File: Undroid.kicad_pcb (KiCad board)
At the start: 4 copper layers, 64.1 x 143 mm, 0 parts

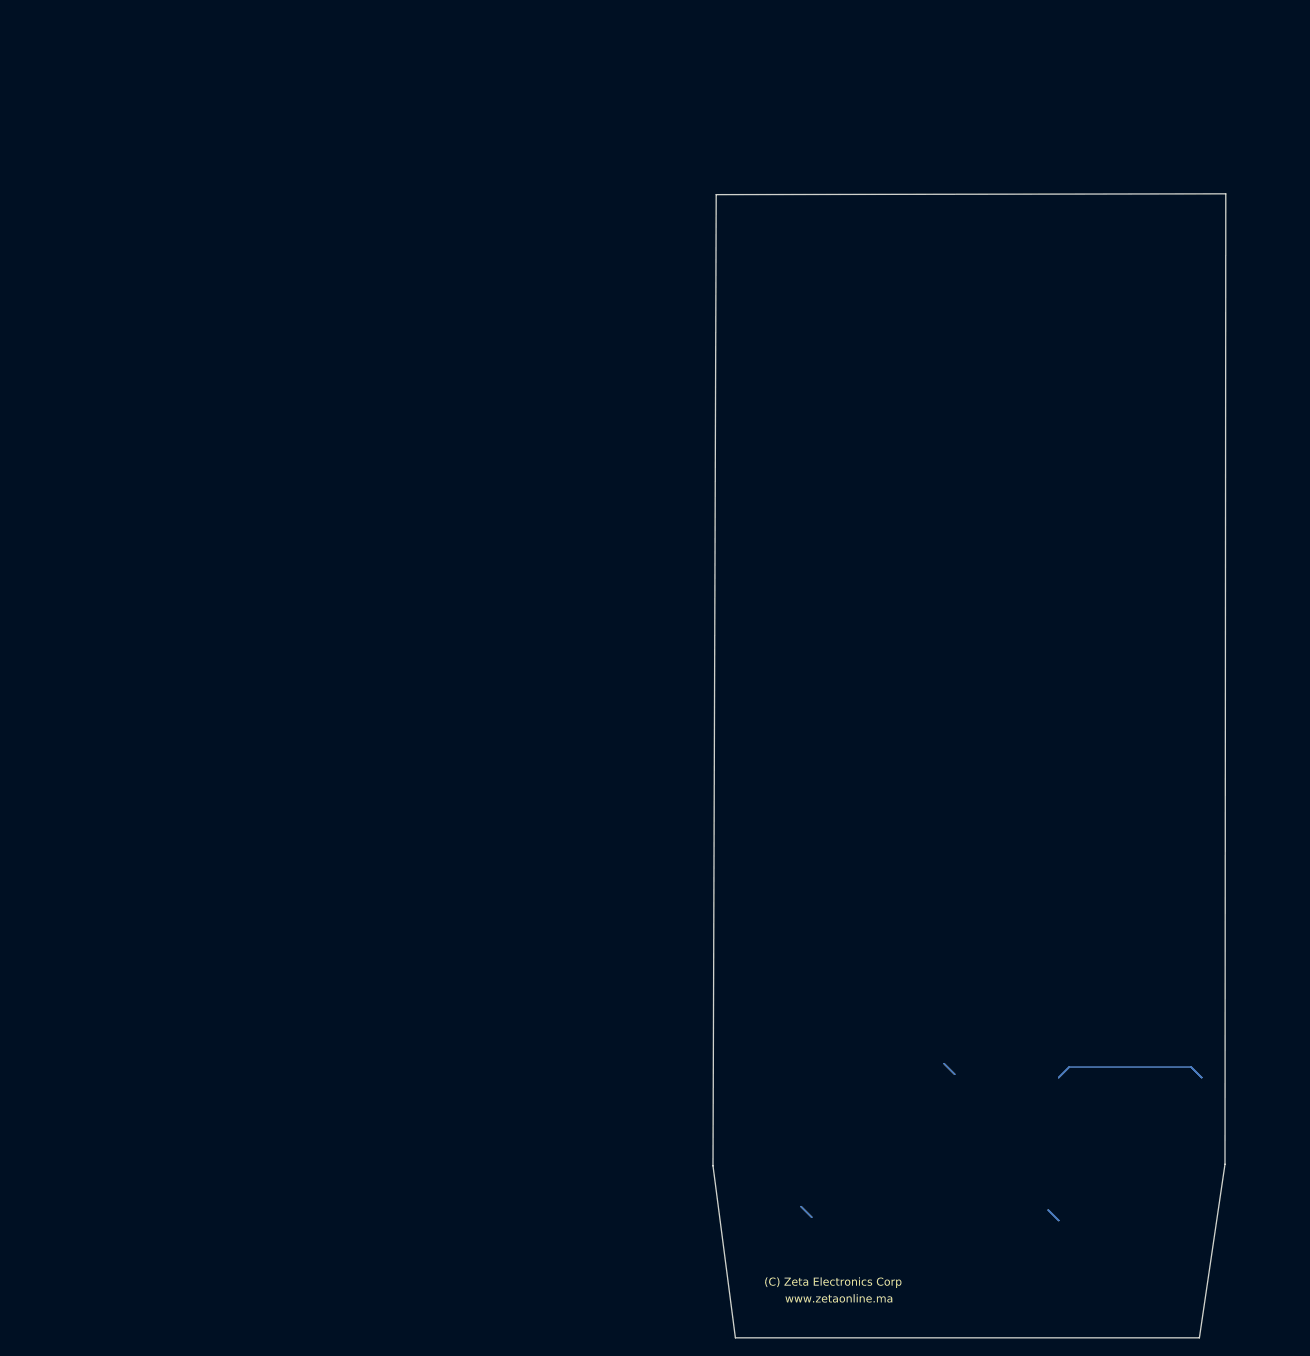
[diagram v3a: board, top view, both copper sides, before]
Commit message: fix: Include part of Allwinner SoC. fix: Fix ERC and DRC.
Signed-off-by: Amlal EL Mahrouss <amlalelmahrouss@icloud.com>
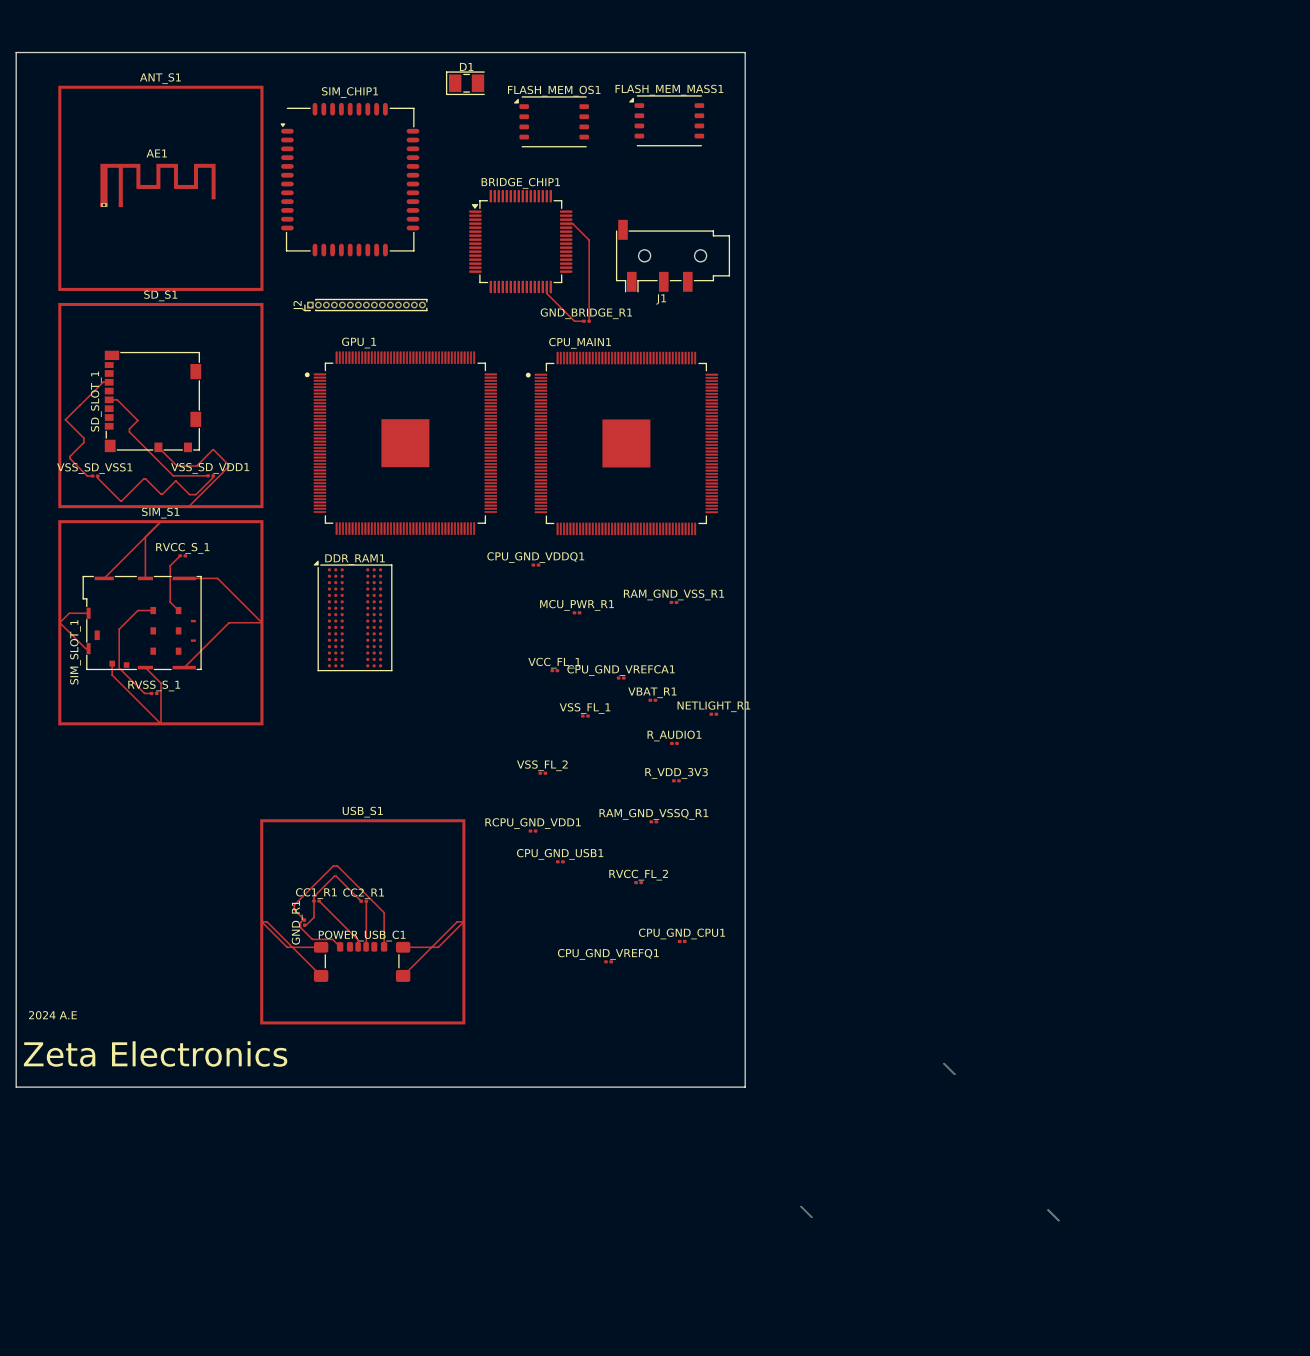
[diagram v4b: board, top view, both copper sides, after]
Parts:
- added AE1: Antenna_Shield, RF_Antenna:Texas_SWRA117D_2.4GHz_Right, F.Cu at (36.7, 39.8)
- added ANT_S1: RFShield_OnePiece, RF_Shielding:Laird_Technologies_97-2002_25.40x25.40mm, F.Cu at (41.7, 37.7)
- added BRIDGE_CHIP1: ATSAME70J19A-AN, Package_QFP:LQFP-64_10x10mm_P0.5mm, F.Cu at (86.7, 44.4)
- added CC1_R1: R, Resistor_SMD:R_0201_0603Metric, F.Cu at (61.1, 126.8)
- added CC2_R1: R, Resistor_SMD:R_0201_0603Metric, F.Cu at (67.0, 126.8)
- added CPU_GND_CPU1: R, Resistor_SMD:R_0201_0603Metric, F.Cu at (106.8, 131.8)
- added CPU_GND_USB1: R, Resistor_SMD:R_0201_0603Metric, F.Cu at (91.6, 121.9)
- added CPU_GND_VDDQ1: R, Resistor_SMD:R_0201_0603Metric, F.Cu at (88.6, 84.8)
- added CPU_GND_VREFCA1: R, Resistor_SMD:R_0201_0603Metric, F.Cu at (99.2, 98.9)
- added CPU_GND_VREFQ1: R, Resistor_SMD:R_0201_0603Metric, F.Cu at (97.6, 134.4)
- added CPU_MAIN1: Allwinner-A13, Allwinner:QFP40P2200X2200X160-177N, F.Cu at (99.9, 69.6)
- added D1: LED, LED_SMD:LED_PLCC-2_3x2mm_AK, F.Cu at (79.9, 24.6)
- added DDR_RAM1: AS4C256M16D3, Package_BGA:BGA-96_9.0x13.0mm_Layout2x3x16_P0.8mm, F.Cu at (66.0, 91.4)
- added FLASH_MEM_MASS1: XTSD08G, Package_LGA:LGA-8_8x6mm_P1.27mm, F.Cu at (105.2, 29.3)
- added FLASH_MEM_OS1: XTSD08G, Package_LGA:LGA-8_8x6mm_P1.27mm, F.Cu at (90.8, 29.4)
- added GND_BRIDGE_R1: R, Resistor_SMD:R_0201_0603Metric, F.Cu at (94.9, 54.3)
- added GND_R1: R, Resistor_SMD:R_0201_0603Metric, F.Cu at (59.6, 129.5)
- added GPU_1: Allwinner-A13, Allwinner:QFP40P2200X2200X160-177N, F.Cu at (72.2, 69.6)
- added J1: AudioJack2, Connector_Audio:Jack_3.5mm_PJ320D_Horizontal, F.Cu at (104.4, 46.1)
- added J2: Conn_01x15, Connector_PinHeader_1.00mm:PinHeader_1x15_P1.00mm_Vertical, F.Cu at (60.4, 52.3)
- added MCU_PWR_R1: R, Resistor_SMD:R_0201_0603Metric, F.Cu at (93.7, 90.8)
- added NETLIGHT_R1: R, Resistor_SMD:R_0201_0603Metric, F.Cu at (110.8, 103.5)
- added POWER_USB_C1: USB_C_Receptacle_PowerOnly_6P, Connector_USB:USB_C_Receptacle_GCT_USB4135-GF-A_6P_TopMnt_Horizontal, F.Cu at (66.8, 135.6)
- added RAM_GND_VSSQ_R1: R, Resistor_SMD:R_0201_0603Metric, F.Cu at (103.3, 116.9)
- added RAM_GND_VSS_R1: R, Resistor_SMD:R_0201_0603Metric, F.Cu at (105.8, 89.5)
- added RCPU_GND_VDD1: R, Resistor_SMD:R_0201_0603Metric, F.Cu at (88.2, 118.0)
- added RVCC_FL_2: R, Resistor_SMD:R_0201_0603Metric, F.Cu at (101.4, 124.5)
- added RVCC_S_1: R, Resistor_SMD:R_0201_0603Metric, F.Cu at (44.4, 83.7)
- added RVSS_S_1: R, Resistor_SMD:R_0201_0603Metric, F.Cu at (40.9, 100.8)
- added R_AUDIO1: R, Resistor_SMD:R_0201_0603Metric, F.Cu at (105.9, 107.1)
- added R_VDD_3V3: R, Resistor_SMD:R_0201_0603Metric, F.Cu at (106.1, 111.8)
- added SD_S1: RFShield_OnePiece, RF_Shielding:Laird_Technologies_97-2002_25.40x25.40mm, F.Cu at (41.7, 64.9)
- added SD_SLOT_1: Micro_SD_Card, Connector_Card:microSD_HC_Molex_104031-0811, F.Cu at (40.7, 64.3)
- added SIM_CHIP1: SIM7020C, RF_GSM:SIMCom_SIM800C, F.Cu at (65.3, 36.6)
- added SIM_S1: RFShield_OnePiece, RF_Shielding:Laird_Technologies_97-2002_25.40x25.40mm, F.Cu at (41.7, 92.0)
- added SIM_SLOT_1: JAE_SIM_Card_SF72S006, Connector_JAE:JAE_SIM_Card_SF72S006, F.Cu at (41.4, 93.0)
- added USB_S1: RFShield_OnePiece, RF_Shielding:Laird_Technologies_97-2002_25.40x25.40mm, F.Cu at (66.9, 129.4)
- added VBAT_R1: R, Resistor_SMD:R_0201_0603Metric, F.Cu at (103.2, 101.7)
- added VCC_FL_1: R, Resistor_SMD:R_0201_0603Metric, F.Cu at (90.9, 98.0)
- added VSS_FL_1: R, Resistor_SMD:R_0201_0603Metric, F.Cu at (94.8, 103.7)
- added VSS_FL_2: R, Resistor_SMD:R_0201_0603Metric, F.Cu at (89.4, 110.8)
- added VSS_SD_VDD1: R, Resistor_SMD:R_0201_0603Metric, F.Cu at (47.9, 73.7)
- added VSS_SD_VSS1: R, Resistor_SMD:R_0201_0603Metric, F.Cu at (33.5, 73.7)
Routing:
- net Net-(SIM_S1-Shield): track 0.00 -> 68.9 mm
- net Net-(POWER_USB_C1-SHIELD): track 0.00 -> 38.3 mm
- net Net-(GND_R1-Pad2): track 0.00 -> 29.6 mm
- net Net-(SD1-SHIELD): track 26.4 -> 0.00 mm
- net GND: track 0.00 -> 26.3 mm
- net VBUS_USBC: track 0.00 -> 20.3 mm
- net Net-(SD_S1-Shield): track 0.00 -> 18.8 mm
- net Net-(SD_SLOT_1-VDD): track 0.00 -> 18.6 mm
- net Net-(SD_SLOT_1-VSS): track 0.00 -> 17.7 mm
- net Net-(SIM_SLOT_1-GND): track 0.00 -> 15.4 mm
- net (no net): track 0.00 -> 11.2 mm
- net Net-(SIM_SLOT_1-VCC): track 0.00 -> 7.79 mm
- net Net-(POWER_USB_C1-CC1): track 0.00 -> 7.75 mm
- net Net-(POWERC1-SHIELD): track 7.44 -> 0.00 mm
- net Net-(BRIDGE_CHIP1-GND-Pad14): track 0.00 -> 6.90 mm
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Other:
- board size 64.1 x 143 mm -> 91.1 x 129.3 mm
- copper layers 4 -> 2
- board text added: "2024 A.E"
- board text added: "Zeta Electronics"
- board text removed: "(C) Zeta Electronics Corp"
- board text removed: "www.zetaonline.ma"

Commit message: pcb: Fix PCB layout.
Signed-off-by: Amlal EL Mahrouss <amlalelmahrouss@icloud.com>
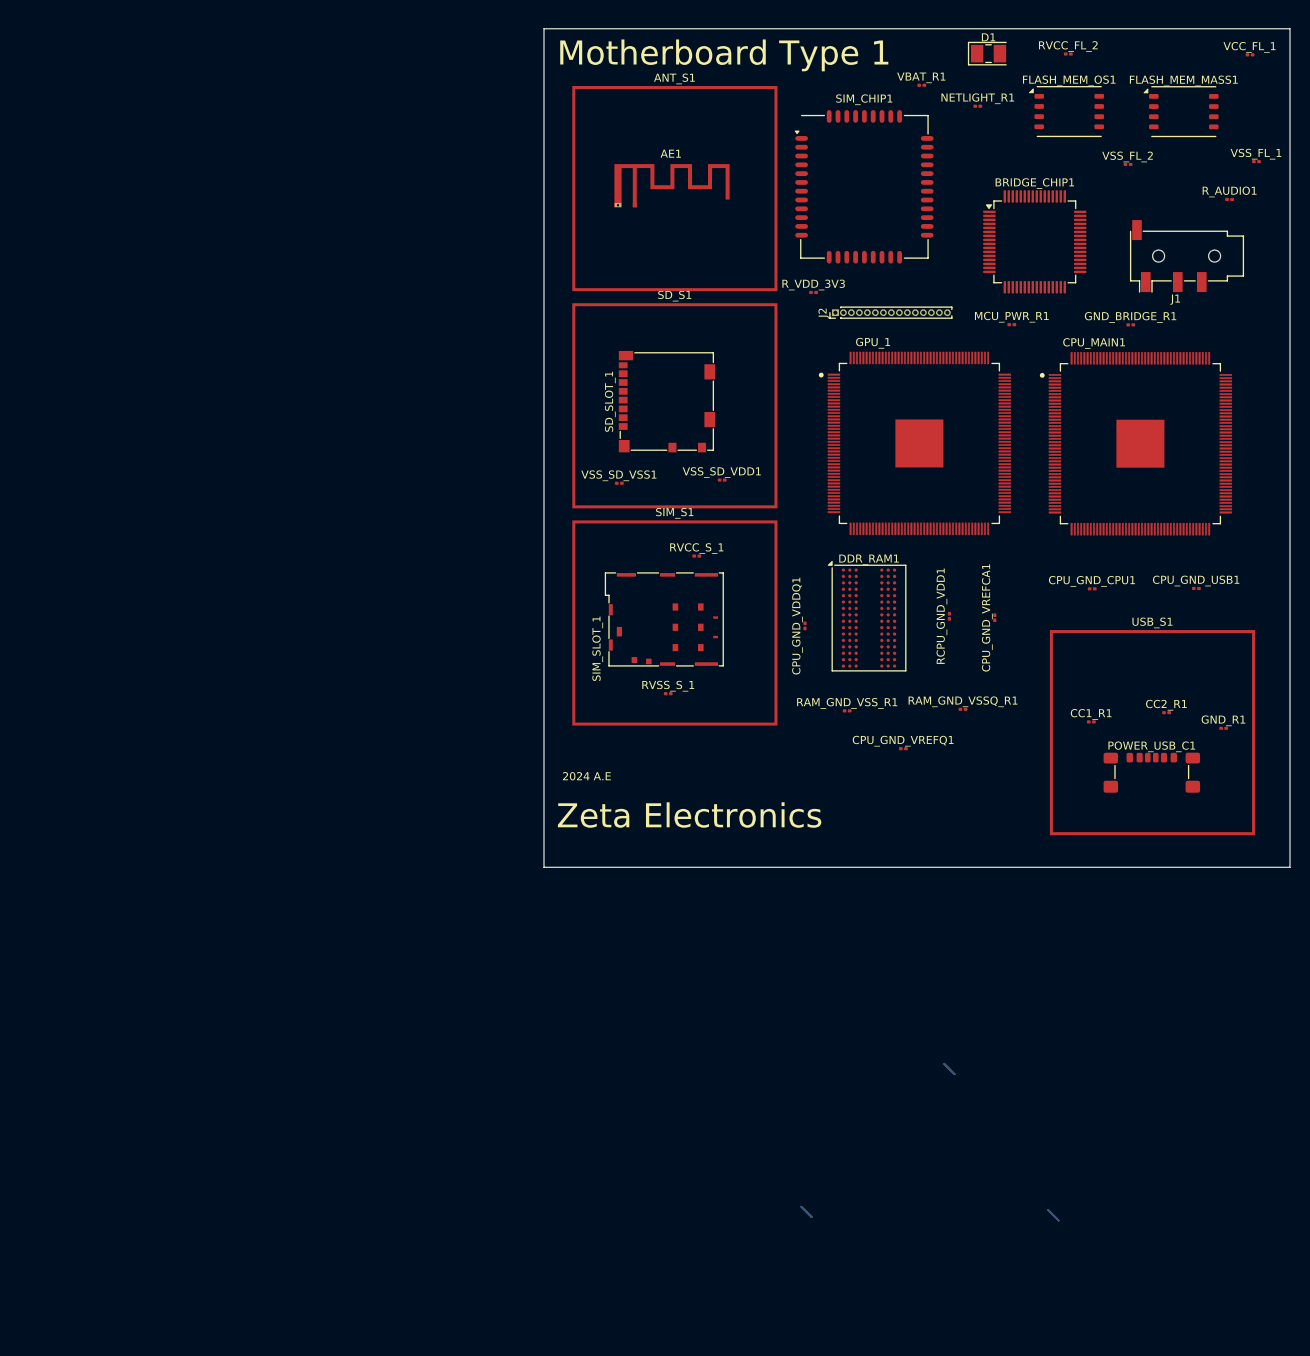
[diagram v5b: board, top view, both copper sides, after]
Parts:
- moved GND_R1 117.4 mm to (174.5, 105.2), turned to 0 degrees
- moved RVCC_FL_2 116.7 mm to (155.1, 20.9)
- moved VCC_FL_1 116.1 mm to (177.8, 21.0)
- moved VSS_FL_1 108.8 mm to (178.6, 34.4)
- moved VSS_FL_2 105.6 mm to (162.6, 34.7)
- moved CC2_R1 103.1 mm to (167.4, 103.3)
- moved POWER_USB_C1 101.5 mm to (165.6, 111.9)
- moved USB_S1 101.5 mm to (165.6, 105.7)
- moved CC1_R1 99.4 mm to (158.0, 104.4)
- moved R_AUDIO1 97.2 mm to (175.3, 39.1)
- moved CPU_GND_USB1 86.5 mm to (171.1, 87.7)
- moved VBAT_R1 83.9 mm to (136.8, 24.8)
- moved NETLIGHT_R1 82.9 mm to (143.8, 27.4)
- moved GND_BRIDGE_R1 68.0 mm to (162.9, 54.8)
- moved CPU_GND_CPU1 67.6 mm to (158.1, 87.8)
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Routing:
- net Net-(SIM_S1-Shield): track 68.9 -> 0.00 mm
- net Net-(POWER_USB_C1-SHIELD): track 38.3 -> 0.00 mm
- net Net-(GND_R1-Pad2): track 29.6 -> 0.00 mm
- net GND: track 26.3 -> 0.00 mm
- net VBUS_USBC: track 20.3 -> 0.00 mm
- net Net-(SD_S1-Shield): track 18.8 -> 0.00 mm
- net Net-(SD_SLOT_1-VDD): track 18.6 -> 0.00 mm
- net Net-(SD_SLOT_1-VSS): track 17.7 -> 0.00 mm
- net Net-(SIM_SLOT_1-GND): track 15.4 -> 0.00 mm
- net Net-(SIM_SLOT_1-VCC): track 7.79 -> 0.00 mm
- net Net-(POWER_USB_C1-CC1): track 7.75 -> 0.00 mm
- net Net-(BRIDGE_CHIP1-GND-Pad14): track 6.90 -> 0.00 mm
- net Net-(POWER_USB_C1-CC2): track 5.68 -> 0.00 mm
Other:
- board size 91.1 x 129.3 mm -> 93.2 x 104.8 mm
- board text added: "Motherboard Type 1"

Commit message: pcb-master: Update prototype.
Signed-off-by: Amlal EL Mahrouss <amlalelmahrouss@icloud.com>
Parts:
- removed AE1: Antenna_Shield, RF_Antenna:Texas_SWRA117D_2.4GHz_Right
- removed ANT_S1, SD_S1, SIM_S1, USB_S1: RFShield_OnePiece, RF_Shielding:Laird_Technologies_97-2002_25.40x25.40mm
- added ANT1: Antenna, RF_Antenna:NiceRF_SW868-TH13_868Mhz, F.Cu at (92.3, 22.1)
- moved J2 59.9 mm to (132.5, 112.8)
- moved D1 19.5 mm to (125.6, 20.4)
- moved RVCC_S_1 12.4 mm to (112.5, 95.5), turned to 90 degrees
- moved CC1_R1 9.19 mm to (157.8, 113.6)
- moved GND_R1 8.93 mm to (177.8, 113.5)
- moved J1 7.21 mm to (175.6, 47.9), turned to 0 degrees
- moved SD_SLOT_1 7.01 mm to (103.3, 71.2)
- moved VSS_SD_VSS1 7.01 mm to (97.4, 81.4)
- moved VSS_SD_VDD1 7.01 mm to (110.2, 81.0)
- moved CC2_R1 6.63 mm to (168.9, 109.7)
- moved POWER_USB_C1 5.65 mm to (168.7, 116.6)
- moved SIM_SLOT_1 5.44 mm to (104.6, 97.6)
- moved RCPU_GND_VDD1 4.96 mm to (142.6, 95.6), turned to 0 degrees
- moved R_VDD_3V3 4.77 mm to (126.7, 54.0)
- moved RVSS_S_1 4.49 mm to (106.3, 105.2)
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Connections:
- POWER_USB_C1 pad S1: Net-(POWER_USB_C1-SHIELD) -> unconnected-(POWER_USB_C1-SHIELD-PadS1)_0
- SD_SLOT_1 pad 9: Net-(SD_S1-Shield) -> unconnected-(SD_SLOT_1-SHIELD-Pad9)
- SIM_SLOT_1 pad SH: Net-(SIM_S1-Shield) -> unconnected-(SIM_SLOT_1-PadSH)_1
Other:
- board size 93.2 x 104.8 mm -> 93.2 x 104.1 mm
- board text added: "DO NOT PUT ELECTRONICS HERE RESERVED SPACE."
- board text added: "DO NOT PUT ELECTRONICS HERE RISK OF GETTING BAD SIGNALS!"
- board text added: "NOTE: MCU/BRIDGE is the Bridge chip."

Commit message: pcb-master: Fix schematic and PCB.
Signed-off-by: Amlal EL Mahrouss <amlalelmahrouss@icloud.com>
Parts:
- moved CPU_GND_VREFQ1 22.3 mm to (118.7, 91.9), turned to 90 degrees
- moved RVCC_S_1 6.83 mm to (112.8, 88.7)
- moved SIM_SLOT_1 6.83 mm to (104.9, 90.8)
- moved RVSS_S_1 6.72 mm to (103.7, 99.0)
- moved CPU_GND_VREFCA1 4.50 mm to (143.3, 92.5)
- moved RAM_GND_VSS_R1 2.42 mm to (125.3, 102.0)
- moved VSS_SD_VDD1 2.26 mm to (108.0, 81.4)
- moved RAM_GND_VSSQ_R1 1.46 mm to (140.7, 102.0)
- moved POWER_USB_C1 1.24 mm to (168.4, 117.8)
- moved RCPU_GND_VDD1 0.96 mm to (143.3, 95.0)
- moved CC2_R1 0.61 mm to (168.3, 109.8)
- moved CPU_GND_USB1 0.18 mm to (171.2, 87.9)
- renumbered CPU_MAIN1 to CPU_1

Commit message: pcb-master: Update PCB.
Signed-off-by: Amlal EL Mahrouss <amlalelmahrouss@icloud.com>
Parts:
- moved J2 47.3 mm to (179.1, 120.9), turned to 180 degrees
- moved CPU_GND_VREFQ1 27.1 mm to (143.1, 80.3), turned to 0 degrees
- moved DDR_RAM1 26.4 mm to (143.3, 68.5)
- moved CPU_GND_VDDQ1 21.3 mm to (143.2, 84.1), turned to 0 degrees
- moved RAM_GND_VSS_R1 19.9 mm to (139.3, 87.9)
- moved CC1_R1 19.1 mm to (157.7, 94.5)
- moved POWER_USB_C1 17.2 mm to (163.0, 101.5)
- moved CC2_R1 15.2 mm to (168.2, 94.6)
- moved GPU_1 13.7 mm to (122.8, 69.4)
- moved SD_SLOT_1 13.5 mm to (98.3, 58.7)
- moved VSS_SD_VSS1 12.8 mm to (95.3, 68.8)
- moved VSS_SD_VDD1 12.8 mm to (105.9, 68.8)
- moved RVCC_S_1 12.3 mm to (109.3, 76.9)
- moved SIM_SLOT_1 11.1 mm to (96.8, 83.1), turned to 180 degrees
- moved GND_R1 9.30 mm to (170.6, 107.7)
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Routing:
- net Net-(DDR_RAM1-VREFCA): track 0.00 -> 22.4 mm, vias 0 -> 2
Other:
- board size 93.2 x 104.1 mm -> 95.9 x 108 mm
- copper layers 2 -> 4
- board text added: "A.E"
- board text added: "VSS_SIM"
- board text removed: "2024 A.E"
- board text removed: "DO NOT PUT ELECTRONICS HERE RESERVED SPACE."
- board text removed: "Motherboard Type 1"
